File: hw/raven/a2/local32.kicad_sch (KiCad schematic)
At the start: 36 parts, among them IC2 PIC16F876A-I_SP, J11 SIMM72, J12 SIMM72, J13 SIMM72, J14 SIMM72, J305 FanHeader, U302 IRF510PBF, U303 TXU0202DCUR, U304 XR68M752, U305 MAX3245CAI+T, X301 24Mhz (3.3V)

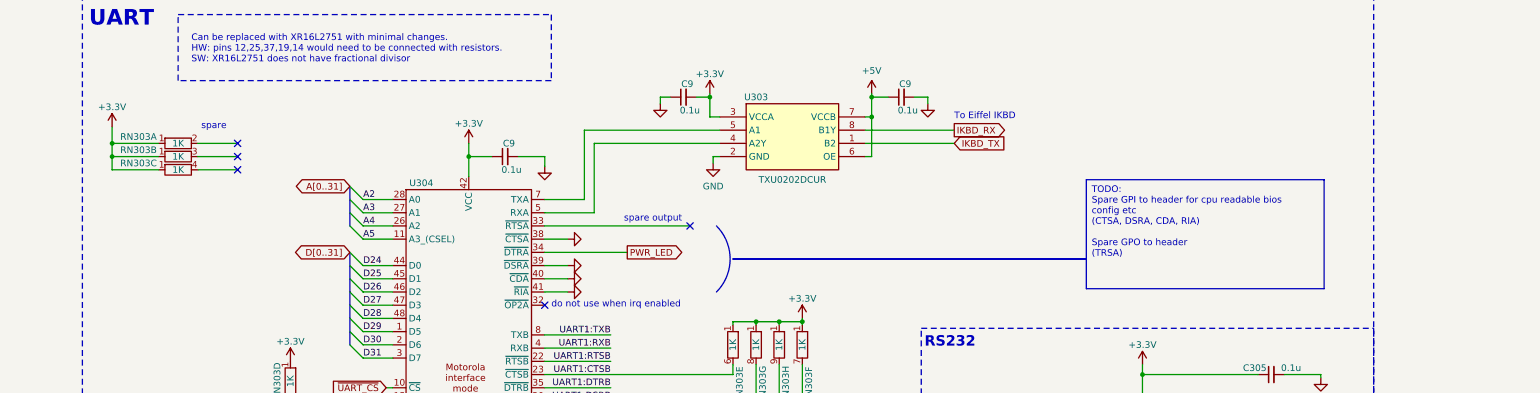
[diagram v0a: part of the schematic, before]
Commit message: Raven.A2 : routing cleanup + gpio
pwr switch status -> uart gpi
uart gpo -> header
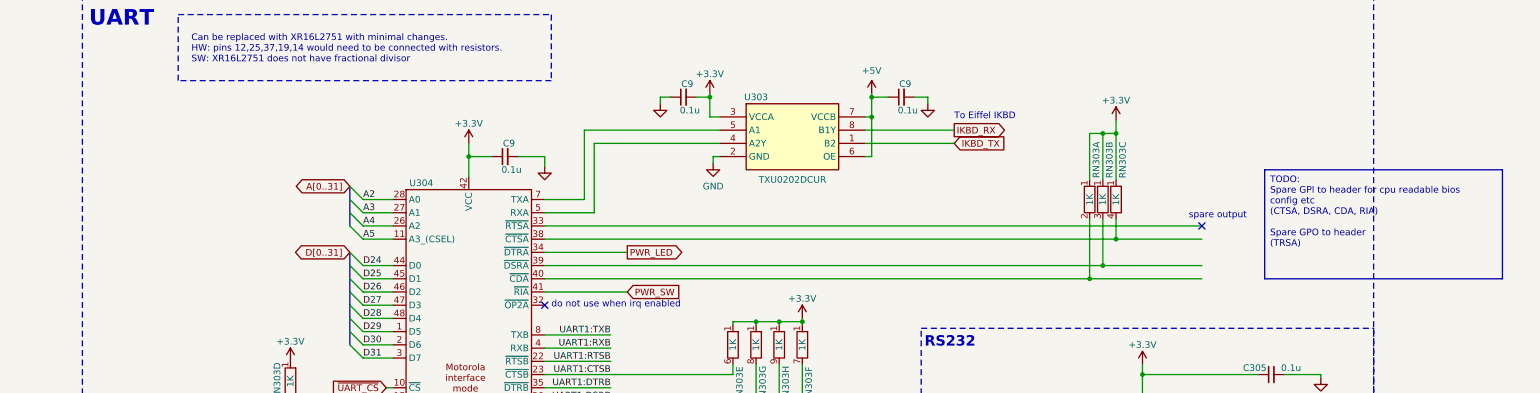
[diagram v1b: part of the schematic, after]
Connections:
- net GND: no longer U304.38 (~{CTSA}), U304.39 (~{DSRA}), U304.40 (~{CDA}), U304.41 (~{RIA})
- net at RN303.2 (R1.2): now also U304.40 (~{CDA})
- net at RN303.3 (R2.2): now also U304.39 (~{DSRA})
- net at RN303.4 (R3.2): now also U304.38 (~{CTSA})
- new net PWR_SW: U304.41 (~{RIA})
- no-connect marks 23 -> 20
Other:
- note removed: "spare"
- moved on the sheet: RN303A, RN303B, RN303C

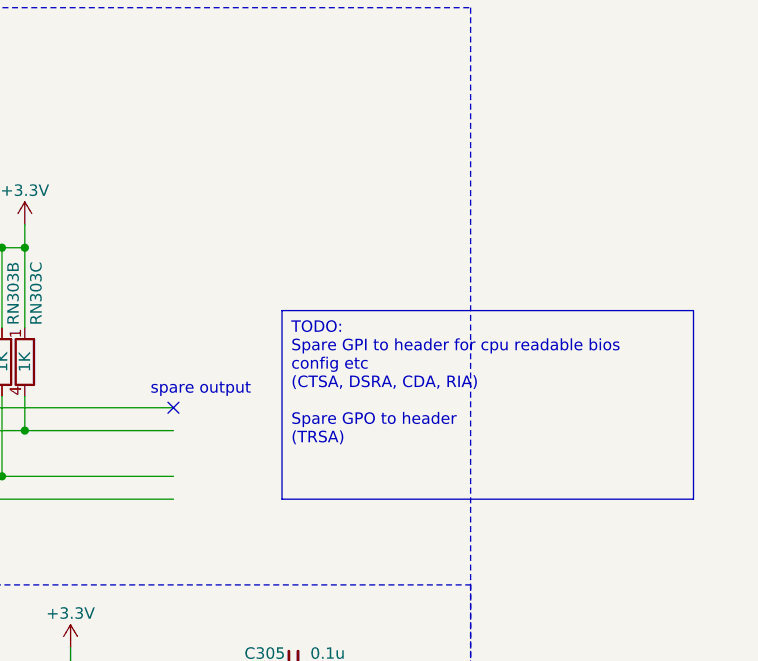
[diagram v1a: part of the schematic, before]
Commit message: rev.A2 updates
Added i2c DAC for reading cpu core temperature
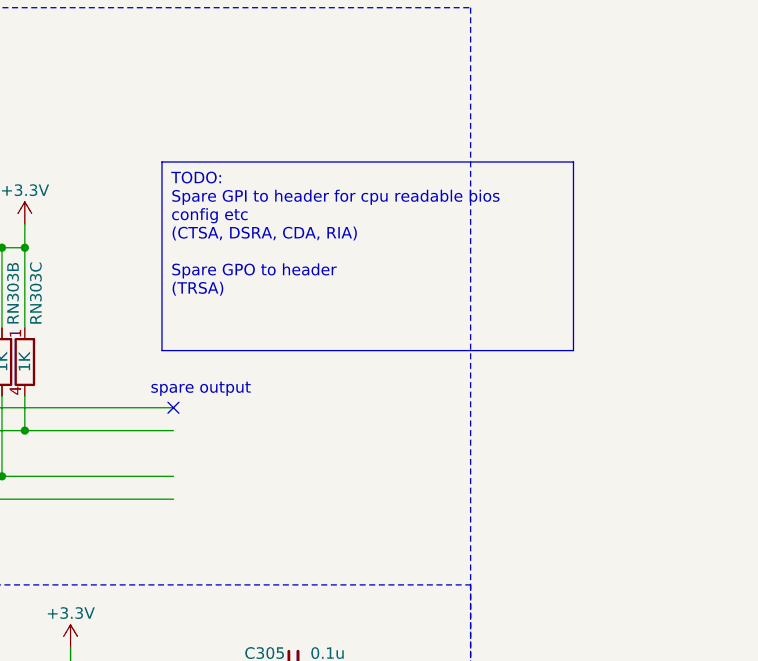
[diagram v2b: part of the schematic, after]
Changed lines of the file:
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@@
   )
   (text_box "TODO:\nSpare GPI to header for cpu readable bios config etc\n(CTSA, DSRA, CDA, RIA)\n\nSpare GPO to header\n(TRSA)\n"
-    (at 539.115 196.215 0) (size 45.72 20.955)
+    (at 525.78 179.705 0) (size 45.72 20.955)
     (stroke (width 0) (type default))
     (fill (type color) (color 255 230 63 0.53))

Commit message: Raven.A2 wip
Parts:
- removed C8: 0.1u, Capacitor_SMD:C_1206_3216Metric_Pad1.33x1.80mm_HandSolder, symbol Device:C_Small
- removed C9 (x2): 0.1u, Capacitor_SMD:C_1206_3216Metric_Pad1.33x1.80mm_HandSolder, symbol 68k:c_100nf_smd1206
- removed IC2: PIC16F876A-I_SP, 68k:DIP794W56P254L3467H406Q28N, symbol 68k:PIC16F876A-I_SP
- removed RN301, RN302: 10K, Resistor_THT:R_Array_SIP9, symbol Device:R_Network08_Split
- removed U303: TXU0202DCUR, 68k:SOP50P310X90-8N, symbol 68k:TXU0202DCUR
- added C308, C309, C310, C311, C312, C313, C314, C315, C316, C317, C318, C319: 0.1u, Capacitor_SMD:C_1206_3216Metric_Pad1.33x1.80mm_HandSolder, symbol 68k:c_100nf_smd1206
- added L301, L302, L303: 120, Inductor_SMD:L_1206_3216Metric_Pad1.42x1.75mm_HandSolder, symbol Device:L_Small
- added R311, R312, R314, R324, R326, R327, R328, R329, R330, R331, R332, R333, R334, R335, R336, R337: 10K, Resistor_SMD:R_1206_3216Metric_Pad1.30x1.75mm_HandSolder, symbol Device:R
- added R316, R317, R318, R319: 49.9, Resistor_SMD:R_1206_3216Metric_Pad1.30x1.75mm_HandSolder, symbol Device:R
- added R320, R321, R322, R323: 3.3, Resistor_SMD:R_1206_3216Metric_Pad1.30x1.75mm_HandSolder, symbol Device:R
- added R325: 12.3K, Resistor_SMD:R_1206_3216Metric_Pad1.30x1.75mm_HandSolder, symbol Device:R
- added U301: CH559L, Package_QFP:LQFP-48_7x7mm_P0.5mm, symbol 68k:CH559L
- added U303: FE1.1s, Package_SO:SSOP-28_3.9x9.9mm_P0.635mm, symbol 68k:FE1.1s
- added U306: RTL8019AS, 68k:RTL8019AS, symbol 68k:RTL8019AS
- added U307: W5100S-L, Package_QFP:LQFP-48_7x7mm_P0.5mm, symbol 68k:W5100S-L
- renumbered C9 to C301, C305 to C302, C306 to C303, C307 to C304, C308 to C305, C309 to C306, C9 to C307, J12 to J301, J13 to J302, J11 to J303, J14 to J304, R10 to R301, R11 to R302, R12 to R303, R13 to R304, R14 to R305, R15 to R306, R16 to R307, R17 to R308, R18 to R309, R19 to R310, R311 to R313, U304 to U302, U302 to U304
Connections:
- net +3.3V: now also C314.1, C315.1, L303.1, R311.2, R312.2, R314.2, R324.1, R326.1, R327.1, U303.18 (VBUSM), U303.21 (RevA:VDD33O_RevB:VDD33F), U303.26 (~{OVCJ}), U307.24 (3V3D_1), U307.36 (3V3D_2); no longer RN303.1 (R1), RN303.1 (R1)
- net +5V: now also R328.1, R329.1, R330.1, R331.1, R332.1, R333.1, R334.1, R335.1, R336.1, R337.1, U306.17 (VCC), U306.31 (~{SMEMRB}), U306.32 (~{SMEMWB}), U306.47 (VCC), U306.57 (VCC), U306.6 (VCC), U306.65 (JP), U306.70 (VCC), U306.89 (VCC)
- net A2: now also U306.5 (SA0), U307.32 (MOSI/A0)
- net A3: now also U306.7 (SA1), U307.33 (MISO/A1)
- net A4: now also U306.8 (SA2)
- net A5: now also U306.9 (SA3)
- net A6: now also U306.10 (SA4)
- net D24: now also U306.36 (SD0), U307.37 (DAT0)
- net D25: now also U306.37 (SD1), U307.38 (DAT1)
- net D26: now also U306.38 (SD2), U307.39 (DAT2)
- net D27: now also U306.39 (SD3), U307.40 (DAT3)
- net D28: now also U306.40 (SD4), U307.41 (DAT4)
- net D29: now also U306.41 (SD5), U307.42 (DAT5)
- net D30: now also U306.42 (SD6), U307.43 (DAT6)
- net D31: now also U306.43 (SD7), U307.44 (DAT7)
- net GND: now also C308.2, C309.2, C310.2, C311.2, C312.2, C313.2, C314.2, C315.2, C316.2, C317.2, C318.2, C319.2, R325.1, U301.18 (GND), U303.1 (VSS), U306.11 (SA5), U306.12 (SA6), U306.13 (SA7), U306.14 (GND), U306.18 (SA10), U306.19 (SA11), U306.20 (SA12), U306.21 (SA13), U306.22 (SA14), U306.23 (SA15), U306.24 (SA16), U306.25 (SA17), U306.26 (SA18), U306.27 (SA19), U306.28 (GND), U306.44 (GND), U306.52 (GND), U306.83 (GND), U306.86 (GND), U307.1 (GNDA_1), U307.10 (GND_1), U307.16 (GNDA_3), U307.23 (GND_2), U307.25 (MOD0), U307.26 (MOD1), U307.28 (MOD3), U307.30 (SCLK/GND), U307.46 (GND_3), U307.7 (GNDA_2)
- net IKBD_RX: now also U302.7 (TXA), U301.27 (P2.6/A14/RXD1)
- net IKBD_TX: now also U302.5 (RXA), U301.28 (P2.7/A15/TXD1/DA7)
- net PWR_LED: now also R327.2
- net PWR_SW: now also U302.40 (~{CDA}), U301.40 (P0.0/AD0/UDTR); no longer U302.41 (~{RIA})
- net R~{W}: now also U307.35 (WRN)
- net ~{IRQ_UART}: now also R326.2; no longer RN303.5 (R4.2)
- net ~{RESET}: now also U307.48 (RSTN)
- net J0DOWN: now reaches R302.2
- net J0DOWN: now also R329.2, U301.19 (DA1/P4.1)
- net J1RIGHT: now reaches R309.2
- net J1RIGHT: now also R336.2, U301.24 (P2.3/A11/SCK1)
- net J0LEFT: now reaches R303.2
- net J0LEFT: now also R330.2, U301.15 (PWM3_/CAP3_/DA2/P4.2), U301.9 (LED1/!A15/INT1/P3.3)
- net J0UP: now reaches R301.2
- net J0UP: now also R328.2, U301.20 (LED2/RXD1_/DA0/P4.0), U301.8 (LED0/INT0/P3.2)
- net J1LEFT: now reaches R308.2
- net J1LEFT: now also R335.2, U301.23 (P2.2/A10/MISO1)
- net at RN303.2 (R1.2): no longer U302.40 (~{CDA})
- net J1UP: now reaches R306.2
- net J1UP: now also R333.2, U301.21 (P2.0/A8)
- net IKBD_GPIO: now reaches RN303.3 (R2.2), U302.39 (~{DSRA})
- net IKBD_GPIO: now also U301.37 (P0.3/AD3/TXD_)
- net TEMP1: now reaches TH301.1
- net TEMP1: now also R314.1, U301.43 (P1.0/AIN0/T1/CAP1)
- net FAN1: now reaches R313.2
- net FAN1: now also U301.10 (LEDC/XCS0/T0/P3.4)
- net J1DOWN: now reaches R307.2
- net J1DOWN: now also R334.2, U301.22 (P2.1/A9/MOSI1)
- net J0BTN1: now reaches R305.2
- net J0BTN1: now also R332.2, U301.6 (LED3/TNOW_/TXD1_/DA4/P4.4)
- net J0RIGHT: now reaches R304.2
- net J0RIGHT: now also R331.2, U301.14 (PWM1_/DA3/P4.3)
- net J1BTN1_J0BTN2: now reaches R310.2
- net J1BTN1_J0BTN2: now also R337.2, U301.25 (P2.4/A12/PWM1), U301.5 (PWM2_/DA5/P4.5)
- net IKBD_CTS: now reaches U302.33 (~{RTSA})
- net IKBD_CTS: now also U301.36 (P0.4/AD4/UCTS)
- net IKBD_RTS: now reaches RN303.4 (R3.2), U302.38 (~{CTSA})
- net IKBD_RTS: now also U301.39 (P0.1/AD1/URTS)
- net JOY1:BTN1 renamed JOY0:BTN2
- new net: C318.1, R316.1, R317.1
- new net: C319.1, R318.1, R319.1
- new net: R311.1, U303.17 (~{XRSTJ})
- new net: R325.2, U307.9 (RSET_BG)
- new net: R323.2, U307.5 (RXIN)
- new net: R312.1, U303.19 (BUSJ)
- new net: R321.2, U307.2 (TXON)
- new net: R322.2, U307.6 (RXIP)
- new net: U306.15 (SA8), U306.16 (SA9)
- new net: U301.30 (HM/ALE/XB/P5.4), U303.15 (DMU)
- new net: U301.29 (HP/!A15/XA/P5.5), U303.16 (DPU)
- new net: R324.2, U307.27 (MOD2)
- new net: R320.2, U307.3 (TXOP)
- new net ETH_1V2A: C308.1, L301.1, U307.4 (1V2A)
- new net ETH_1V2D: C310.1, C311.1, C312.1, C313.1, L302.2, U307.13 (1V2D_1), U307.22 (1V2D_2), U307.31 (1V2D_3), U307.45 (1V2D_4)
- new net ETH_1V2O: C309.1, L301.2, L302.1, U307.14 (1V2O)
- new net RJ:LED_GREEN: U307.17 (LNKN)
- new net RJ:LED_YELLOW: U307.20 (ACTN)
- new net RJ:TRD1+: R319.2, R320.1
- new net RJ:TRD1-: R318.2, R321.1
- new net RJ:TRD2+: R317.2, R322.1
- new net RJ:TRD2-: R316.2, R323.1
- new net RJ:VCC: C316.1, C317.1, L303.2, U307.15 (3V3A_2), U307.8 (3V3A_1)
- new net TEMP2: U301.44 (P1.1/AIN1/T2EX/CAP2)
- new net USB1:D+: U301.31 (DP/P5.1)
- new net USB1:D-: U301.32 (DM/P5.0)
- new net USB2:D+: U303.11 (DP1)
- new net USB2:D-: U303.10 (DM1)
- new net ~{ETH_CS}: U307.29 (CSN)
- new net ~{IRQ_ETH}: U302.41 (~{RIA}), U307.47 (INTN)
- no-connect marks 20 -> 89
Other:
- note added: "0000 : SPI Mode 010X : BUS Mode"
- note added: "0; bus powered 1: self powered"
- note added: "12.3k 1% resistor"
- note added: "25Mhz 1.2V"
- note added: "Ethernet"
- note added: "FAN1 : 12V"
- note added: "Keyboard, mouse, joystick IKBD compatible"
- note added: "Not 5V tolerant pin"
- note added: "Optional damping for EMI reduction."
- note added: "RSET_BG is the most important analog pin and users should keep the noisy source away from this pin"
- note added: "TEMP1 : Motherboard"
- note added: "To avoid the 100M overshoot, please place the 49.9 resistors and 0.1uF capacitor near the MDI pin of W5100S"
- note added: "activity led (low/flash: state, high: down)"
- note added: "collision led (low: collision, high: no collision)"
- note added: "duplex led (low: full, high: half)"
- note added: "high = jumper mode"
- note added: "inputs. can trigger MSR interrupt on input changed"
- note added: "internal 100k pulldowns on jumper config pins"
- note added: "internal pullup"
- note added: "irq_hi"
- note added: "irq_lo"
- note added: "jp: brom size, 00xxxx = disabled"
- note added: "jp: io base, 0000 = 0x300"
- note added: "jp: irq line, int0"
- note added: "jp: medium, 00 = auto (10baseT, link test enabled)"
- note added: "jp: pnp mode, don't care in jumper mode"
- note added: "prog"
- note added: "pullup"
- note added: "speed led (low: 100, high: 10)"
- note added: "status led (low: up, high: down)"
- note added: "todo"
- note added: "todo (0x300)"
- note added: "todo (caps)"
- note removed: "5V"
- note removed: "Keyboard, mouse, joystick Eiffel IKBD"
- note removed: "To Eiffel IKBD"
- note removed: "keyb led"
- note removed: "lcd"
- note removed: "mouse led"
- note removed: "spare output"
- moved on the sheet: C301, C302, C303, C304, C305, C306, C307, J305, R301, R302, R303, R304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

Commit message: A2 fan pwm+argb
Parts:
- removed J305: FanHeader, HDRV3W99P0X254_1X3_747X635X843P, symbol 68k:171856-1003
- removed R313: 10K, Resistor_SMD:R_1206_3216Metric_Pad1.30x1.75mm_HandSolder, symbol Device:R
- removed U304: IRF510PBF, Package_TO_SOT_THT:TO-220-3_Horizontal_TabDown, symbol 68k:IRF510PBF
- removed U306: RTL8019AS, 68k:RTL8019AS, symbol 68k:RTL8019AS
- added J306: ARGB, 68k:HDRV4W76P0X254_1X4_1016X254X813P, symbol 68k:fan_argb
- added J307: PWM, 68k:470531000, symbol 68k:fan_pwm
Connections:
- net +12V: now also J307.3 (12V)
- net +5V: now also J306.1 (5V)
- net GND: now also J306.4 (GND), J307.4 (GND)
- net FAN1_PWM: now reaches U301.26 (P2.5/A13/TNOW/PWM2/T2EX_/CAP2_)
- net FAN1_PWM: now also J307.1 (PWM)
- net FAN1 renamed FAN1_ARGB
- net FAN1_ARGB: now also J306.2 (Data)
- no-connect marks 89 -> 45
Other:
- note added: "Fans have built-in 3.3V or 5V pullup resistor on Data pin"
- note removed: "fan"
- note removed: "high = jumper mode"
- note removed: "internal 100k pulldowns on jumper config pins"
- note removed: "jp: brom size, 00xxxx = disabled"
- note removed: "jp: io base, 0000 = 0x300"
- note removed: "jp: irq line, int0"
- note removed: "jp: medium, 00 = auto (10baseT, link test enabled)"
- note removed: "jp: pnp mode, don't care in jumper mode"
- note removed: "todo (0x300)"
- note removed: "todo (caps)"
- moved on the sheet: R311, R312, U303

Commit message: a2 wip
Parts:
- removed R311, R312: 10K, Resistor_SMD:R_1206_3216Metric_Pad1.30x1.75mm_HandSolder, symbol Device:R
- removed RN303: 1K, Resistor_THT:R_Array_SIP9, symbol Device:R_Network08_Split
- removed U303: FE1.1s, Package_SO:SSOP-28_3.9x9.9mm_P0.635mm, symbol 68k:FE1.1s
- added C301, C302, C327: 0.1u, Capacitor_SMD:C_1206_3216Metric_Pad1.33x1.80mm_HandSolder, symbol 68k:c_100nf_smd1206
- added C303, C304, C328, C329: 33p, Capacitor_SMD:C_1206_3216Metric_Pad1.33x1.80mm_HandSolder, symbol 68k:c_100nf_smd1206
- added C306, C307, C309: 10u, Capacitor_SMD:C_1206_3216Metric_Pad1.33x1.80mm_HandSolder, symbol 68k:c_100nf_smd1206
- added J306: Pinhdr_01x03, Connector_PinHeader_2.54mm:PinHeader_1x03_P2.54mm_Vertical, symbol Connector_Generic:Conn_01x03
- added J307: USB2Header, 68k:USB2Header, symbol 68k:USB2Header
- added R301, R317, R324, R325, R329, R330, R331: 1K, Resistor_SMD:R_1206_3216Metric_Pad1.30x1.75mm_HandSolder, symbol Device:R
- added R327, R340: 10K, Resistor_SMD:R_1206_3216Metric_Pad1.30x1.75mm_HandSolder, symbol Device:R
- added R342: 1M, Resistor_SMD:R_1206_3216Metric_Pad1.30x1.75mm_HandSolder, symbol Device:R
- added U302: CH334R, Package_SO:QSOP-16_3.9x4.9mm_P0.635mm, symbol 68k:CH334R
- added U304: CH213K, Package_TO_SOT_SMD:SOT-23-3, symbol 68k:CH213K
- added U307: 74LVC1G19, Package_TO_SOT_SMD:SOT-23-6_Handsoldering, symbol 74xGxx:74LVC1G19
- added Y301: 12Mhz, 68k:ECS120203XENTR, symbol Device:Crystal
- added Y302: 25Mhz, 68k:ECS120203XENTR, symbol Device:Crystal
- renumbered C301 to C305, C302 to C308, C303 to C310, C304 to C311, C307 to C312, C305 to C313, C306 to C314, C308 to C315, C309 to C316, C310 to C317, C311 to C318, C312 to C319, C313 to C320, C314 to C321, C315 to C322, C316 to C323, C317 to C324, C318 to C325, C319 to C326, J307 to J305, J306 to J308, R328 to R302, R329 to R303, R330 to R304, R331 to R305, R332 to R306, R301 to R307, R302 to R308, R303 to R309, R304 to R310, R305 to R311, R333 to R312, R334 to R313, R335 to R314, R336 to R315, R337 to R316, R306 to R318, R307 to R319, R308 to R320, R309 to R321, R310 to R322, R327 to R323, R314 to R326, R326 to R328, R316 to R332, R317 to R333, R318 to R334, R319 to R335, R320 to R336, R321 to R337, R322 to R338, R323 to R339, R324 to R341, R325 to R343, U302 to U303, U307 to U306
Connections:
- net +3.3V: now also U301.41 (VIN5), U301.42 (VDD33), C301.1, C302.2, C327.1, R301.1, R317.1, R324.1, R325.1, R329.1, R330.1, R331.1, R340.1, U307.5 (VCC)
- net +5V: now also C309.1, U304.3 (VI+)
- net GND: now also C301.2, C302.1, C303.2, C304.2, C306.1, C307.1, C309.2, C327.2, C328.2, C329.2, J307.7 (GND), J307.8 (GND), R327.1, U302.14 (GND), U304.1 (GND), U307.2 (GND)
- net IKBD_CTS: now also R325.2
- net IKBD_RTS: now also R301.2
- net IKBD_RX: now also R324.2
- net IKBD_TX: now also R317.2
- net PWR_SW: now also U303.41 (~{RIA}); no longer U303.40 (~{CDA})
- net R~{W}: now also U307.1 (A); no longer U306.35 (WRN)
- net UART1:DTRB: now also R331.2
- net UART1:RTSB: now also R329.2
- net UART1:TXB: now also R330.2
- net USB1:D+: now also U301.29 (HP/!A15/XA/P5.5), U302.11 (DPU); no longer U301.31 (DP/P5.1)
- net USB1:D-: now also U301.30 (HM/ALE/XB/P5.4), U302.10 (DMU); no longer U301.32 (DM/P5.0)
- net USB2:D+: now also U302.8 (DP1)
- net USB2:D-: now also U302.7 (DM1)
- net ~{ETH_CS}: now also U307.3 (~{E})
- net ~{IRQ_ETH}: now also U303.40 (~{CDA}), R340.2; no longer U303.41 (~{RIA})
- net at U306.11 (XSCO): now also C329.1, R342.2, Y302.2
- net at U306.12 (XSCI): now also C328.1, R342.1, Y302.1
- net ~{ETH_RD}: now reaches U306.34 (RDN)
- net ~{ETH_RD}: now also U307.4 (Y1)
- net FAN1_PWR: now reaches U301.11 (DA6/T1/P3.5)
- net ~{DBG:PROG}: now reaches U301.16 (XI/SCS_/P4.6)
- net ~{DBG:PROG}: now also J306.3 (Pin_3)
- net DBG:TX: now reaches U301.7 (TXD/P3.1)
- net DBG:TX: now also J306.1 (Pin_1)
- net IKBD_GPIO: no longer names the net of U303.39 (~{DSRA})
- net IKBD_GPIO: no longer U301.37 (P0.3/AD3/TXD_)
- net J1BTN1_J0BTN2 renamed J1BTN1
- new net: C304.1, U302.15 (XO), Y301.2
- new net: C303.1, U302.16 (XI), Y301.1
- new net: J306.2 (Pin_2), R327.2
- new net USB0:D+: U301.31 (DP/P5.1)
- new net USB0:D-: U301.32 (DM/P5.0)
- new net USB3:D+: J307.5 (DP0), U302.6 (DP2)
- new net USB3:D-: J307.3 (DM0), U302.5 (DM2)
- new net USB4:D+: J307.6 (DP1), U302.4 (DP3)
- new net USB4:D-: J307.4 (DM1), U302.3 (DM3)
- new net USB5:D+: U302.2 (DP4)
- new net USB5:D-: U302.1 (DM4)
- new net VUSB: C306.2, C307.2, J307.1 (+5V), J307.2 (+5V), U304.2 (VO-)
- new net ~{ETH_WR}: U306.35 (WRN), U307.6 (Y0)
- no-connect marks 45 -> 34
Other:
- note added: "(unused on A2)"
- note added: "AutoShutdownPlus Disabled FORCEON = ~{FORCEOFF} = VCC, no load T_OUT = Always active R_OUT = Always active T_IN = has no pullups"
- note added: "DEBUG"
- note added: "Differences from standalone CKBD upgrade: - PWR_SW moved from P0.3 to P0.0 - IKBD_RTS added on P0.1 - IKBD_CTS added on P0.4 - FAN1_PWM added on P2.5 - FAN1_RGB added on P3.4 - FAN1_PWR removed from P3.5 - PS2M removed from P3.2, P3.3 - PS2K removed from P3.6, P3.7 - J0UP added on P3.2 (for irq) - J0LEFT added on P3.3 (for irq)"
- note added: "Fans have built-in 3.3V or 5V pullup resistor on PWM pin"
- note added: "Optional Not included in CH334R datasheet"
- note added: "Or general GPIO between UART and CKBD"
- note added: "Outputs: /RTSA , default 1 /DTRA , default 1 Inputs: /CTSA , MSR irq lo <-> hi /DSRA , MSR irq lo <-> hi /CDA , MSR irq lo <-> hi /RIA , MSR irq lo -> hi"
- note added: "RST has built in pullup resistor. Recommended to leave floating when not reset."
- note added: "RxIN has internal 5k pulldowns RxOUT is inverted output"
- note added: "USB Header"
- note added: "USB hub"
- note added: "Using 3.3V supply voltage: VIN5: Input external 3.3V voltage to voltage regulator, must be grounded to not less than 0.1uF decoupling capacitor VDD33: Input external 3.3V as internal working power supply, must be grounded to not less than 0.1uF decoupling capacitor"
- note added: "Using 5V supply voltage: VIN5: Input external 5V voltage to voltage regulator, must be grounded to not less than 0.1uF decoupling capacitor VDD33: Internal voltage regulator 3.3V output and 3.3V internal working power input, must be grounded to not less than 3.3uF decoupling capacitor"
- note added: "VBUS"
- note added: "dbg header"
- note added: "internal oscillator: remove Y301 remove C304 0 ohm resistor on C303"
- note removed: "0; bus powered 1: self powered"
- note removed: "AutoShutdownPlus Disabled FORCEON = ~{FORCEOFF} = VCC, no load"
- note removed: "Fans have built-in 3.3V or 5V pullup resistor on Data pin"
- note removed: "inputs. can trigger MSR interrupt on input changed"
- note removed: "internal pullup"
- note removed: "pullup"
- note removed: "todo"
- moved on the sheet: C308, C310, C311, C312, C313, C314, J308, R302, R303, R304, R305, R306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

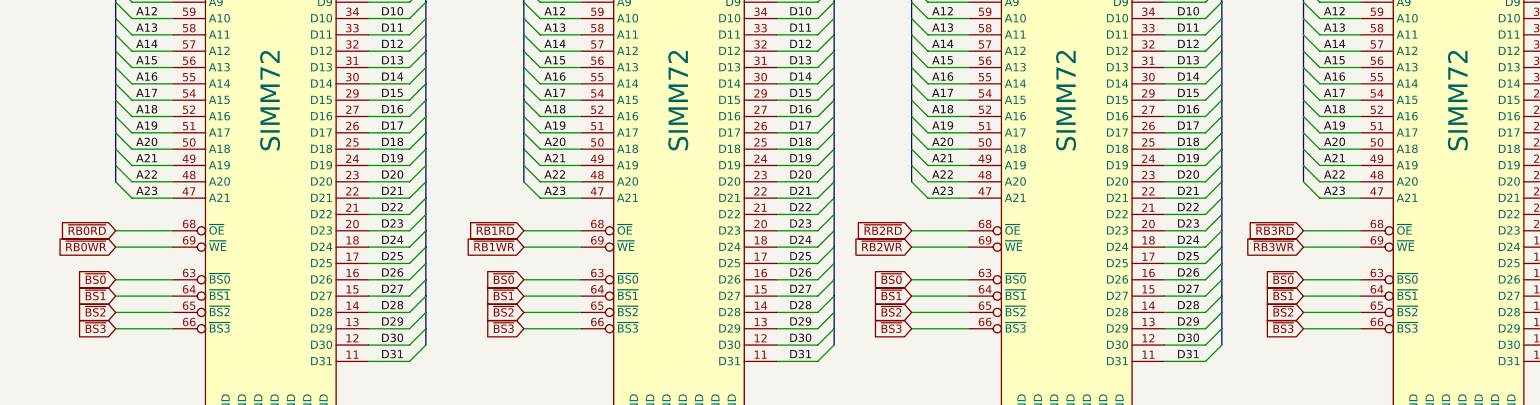
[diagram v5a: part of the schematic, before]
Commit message: A2: support 32MB simms
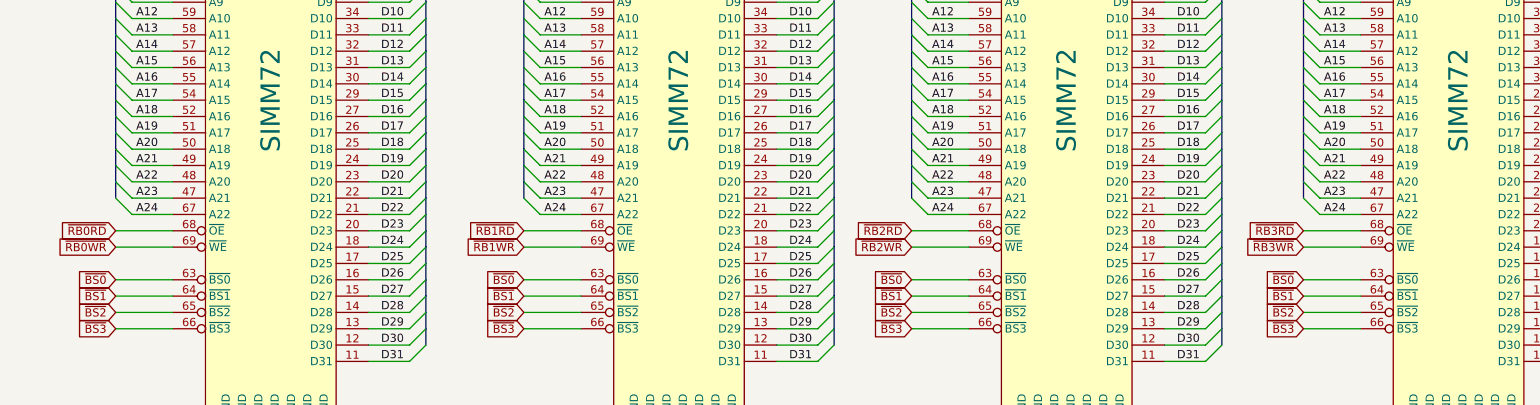
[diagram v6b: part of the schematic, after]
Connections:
- net A24: now reaches J301.67 (A22)
- net A24: now also J302.67 (A22), J303.67 (A22), J304.67 (A22)
